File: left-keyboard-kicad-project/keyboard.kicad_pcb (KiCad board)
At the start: 2 copper layers, 180 x 155.4 mm, 78 parts, among them U1 Arduino_Pro_Micro, U2 TRRS

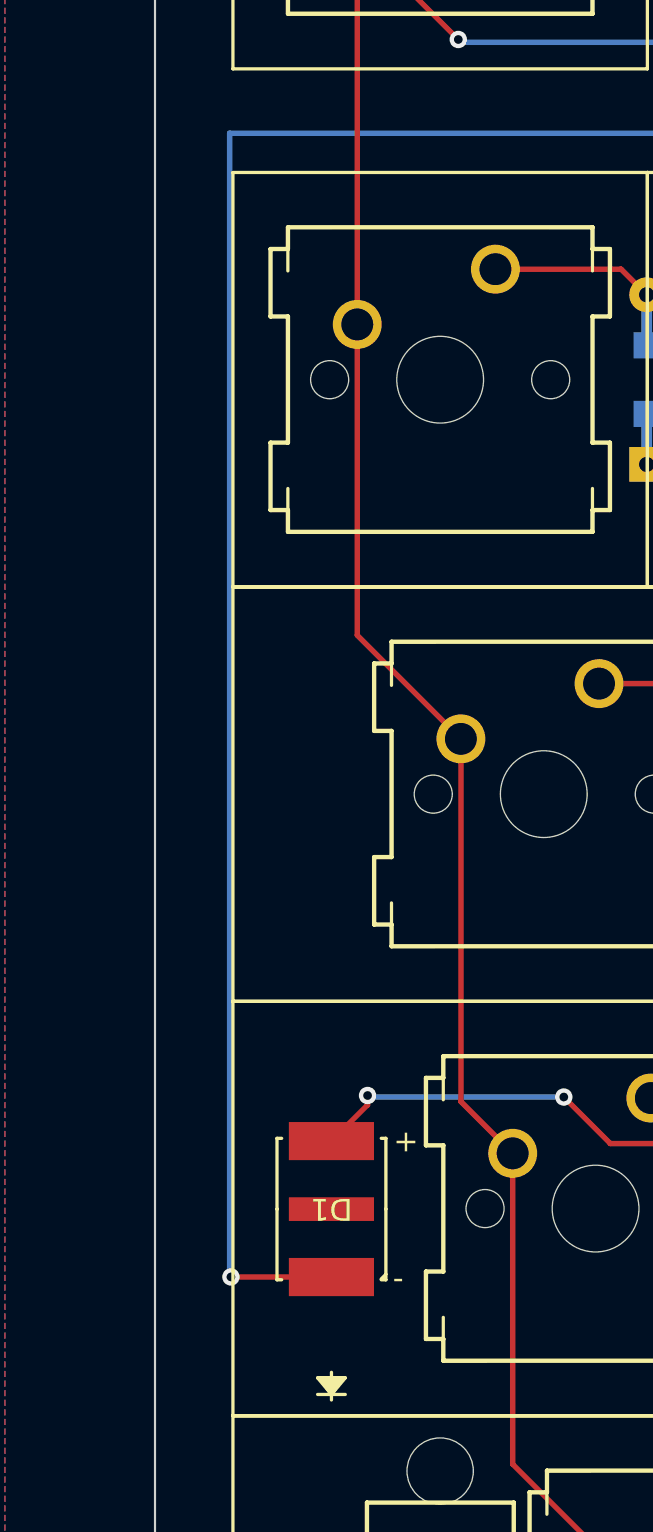
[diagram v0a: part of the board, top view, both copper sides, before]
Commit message: update left keyboard to have slightly shifted LED
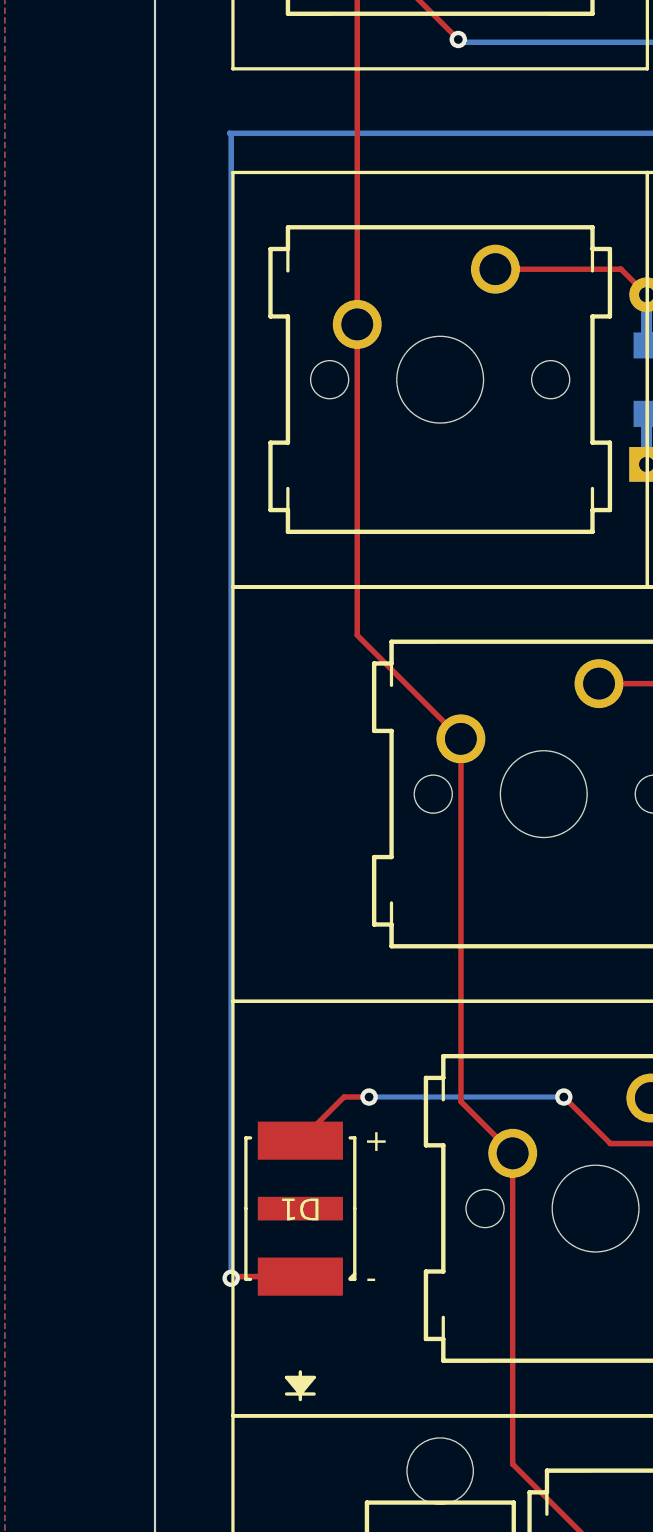
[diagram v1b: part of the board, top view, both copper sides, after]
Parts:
- moved D1 1.43 mm to (51.7, 104.7)
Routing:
- net GND: track 234.0 -> 232.6 mm
- net Net-(D1-A): track 27.8 -> 28.9 mm
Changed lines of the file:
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@@
   )
   (footprint "MX6AWT_A1_0000_000D51 footprint:LED_CREE_MX6" (layer "F.Cu")
-    (at 53.11 104.6794 180)
+    (at 51.68 104.6594 180)
     (tags "MX6AWT-A1-0000-000D51 ")
     (property "Sheetfile" "keyboard.kicad_sch")
@@
   (gr_line (start 212.5 70) (end 197.5 70)
     (stroke (width 0.1) (type default)) (layer "Edge.Cuts"))
-  (gr_text "+" (at 55.96 102.15) (layer "F.SilkS")
+  (gr_text "+" (at 54.6 102.13) (layer "F.SilkS")
     (effects (font (size 1 1) (thickness 0.15)) (justify left bottom))
   )
-  (gr_text "-" (at 55.93 108.44) (layer "F.SilkS")
+  (gr_text "-" (at 54.69 108.43) (layer "F.SilkS")
     (effects (font (size 1 1) (thickness 0.15)) (justify left bottom))
   )
   (segment (start 76.9 101.67) (end 65.93 101.67) (width 0.25) (layer "F.Cu") (net 1))
   (segment (start 65.93 101.67) (end 63.79 99.53) (width 0.25) (layer "F.Cu") (net 1))
-  (segment (start 54.77 99.46) (end 54.77 99.8952) (width 0.25) (layer "F.Cu") (net 1))
-  (segment (start 54.77 99.8952) (end 53.11 101.5552) (width 0.25) (layer "F.Cu") (net 1))
+  (segment (start 51.68 101.5352) (end 53.6852 99.53) (width 0.25) (layer "F.Cu") (net 1))
+  (segment (start 53.6852 99.53) (end 54.84 99.53) (width 0.25) (layer "F.Cu") (net 1))
+  (via (at 54.84 99.53) (size 0.8) (drill 0.4) (layers "F.Cu" "B.Cu") (net 1))
   (via (at 63.79 99.53) (size 0.8) (drill 0.4) (layers "F.Cu" "B.Cu") (net 1))
   (via (at 76.9 101.67) (size 0.8) (drill 0.4) (layers "F.Cu" "B.Cu") (net 1))
-  (via (at 54.77 99.46) (size 0.8) (drill 0.4) (layers "F.Cu" "B.Cu") (net 1))
   (segment (start 76.9 103.68) (end 76.9 101.67) (width 0.25) (layer "B.Cu") (net 1))
   (segment (start 63.79 99.53) (end 54.84 99.53) (width 0.25) (layer "B.Cu") (net 1))
-  (segment (start 54.84 99.53) (end 54.77 99.46) (width 0.25) (layer "B.Cu") (net 1))
   (segment (start 85.527525 61.477525) (end 86.68 62.63) (width 0.25) (layer "F.Cu") (net 2))
   (segment (start 79.697071 61.477525) (end 85.527525 61.477525) (width 0.25) (layer "F.Cu") (net 2))
@@
   (segment (start 208.485 46.025) (end 217.375 46.025) (width 0.25) (layer "F.Cu") (net 57))
   (segment (start 212.24 44.7) (end 207.5 39.96) (width 0.25) (layer "F.Cu") (net 60))
+  (segment (start 48.5764 107.7836) (end 51.68 107.7836) (width 0.25) (layer "F.Cu") (net 60))
   (segment (start 192.26 42.5) (end 192.26 45.04) (width 0.25) (layer "F.Cu") (net 60))
   (segment (start 204.96 42.5) (end 192.26 42.5) (width 0.25) (layer "F.Cu") (net 60))
-  (segment (start 48.49 107.8) (end 48.4936 107.8036) (width 0.25) (layer "F.Cu") (net 60))
   (segment (start 215.2 44.7) (end 212.24 44.7) (width 0.25) (layer "F.Cu") (net 60))
-  (segment (start 48.4936 107.8036) (end 53.11 107.8036) (width 0.25) (layer "F.Cu") (net 60))
   (segment (start 207.5 39.96) (end 204.96 42.5) (width 0.25) (layer "F.Cu") (net 60))
   (segment (start 185.3 45.04) (end 185.27 45.07) (width 0.25) (layer "F.Cu") (net 60))
+  (segment (start 48.5 107.86) (end 48.5764 107.7836) (width 0.25) (layer "F.Cu") (net 60))
   (segment (start 192.26 45.04) (end 185.3 45.04) (width 0.25) (layer "F.Cu") (net 60))
   (via (at 185.27 45.07) (size 0.8) (drill 0.4) (layers "F.Cu" "B.Cu") (net 60))
-  (via (at 48.49 107.8) (size 0.8) (drill 0.4) (layers "F.Cu" "B.Cu") (net 60))
+  (via (at 48.5 107.86) (size 0.8) (drill 0.4) (layers "F.Cu" "B.Cu") (net 60))
   (segment (start 185.27 45.07) (end 185.27 45.43) (width 0.25) (layer "B.Cu") (net 60))
   (segment (start 185.27 45.43) (end 175.47 55.23) (width 0.25) (layer "B.Cu") (net 60))
   (segment (start 175.47 55.23) (end 48.43 55.23) (width 0.25) (layer "B.Cu") (net 60))
-  (segment (start 48.43 55.23) (end 48.43 107.74) (width 0.25) (layer "B.Cu") (net 60))
-  (segment (start 48.43 107.74) (end 48.49 107.8) (width 0.25) (layer "B.Cu") (net 60))
+  (segment (start 48.5 55.3) (end 48.5 107.86) (width 0.25) (layer "B.Cu") (net 60))
+  (segment (start 48.43 55.23) (end 48.5 55.3) (width 0.25) (layer "B.Cu") (net 60))
   (zone (net 0) (net_name "") (layers "F&B.Cu") (hatch edge 0.5)
     (connect_pads (clearance 0.508))

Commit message: update left keyboard
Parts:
- moved U2 1.85 mm to (219.3, 33.4)
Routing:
- net Net-(U1-VCC): track 13.7 -> 15.6 mm
- net Net-(U1-RX1/PD2): track 30.9 -> 32.7 mm
- net Net-(U1-TX0/PD3): track 28.4 -> 30.3 mm
- net GND: track 232.6 -> 231.3 mm
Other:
- board text added: "Designed by Kyle Chiu"
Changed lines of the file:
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@@
   )
   (footprint "ScottoKeebs_Components:TRRS_PJ-320A" (layer "F.Cu")
-    (at 217.5 33.4)
+    (at 219.35 33.3775)
     (property "Sheetfile" "keyboard.kicad_sch")
     (property "Sheetname" "")
@@
   (gr_line (start 212.5 70) (end 197.5 70)
     (stroke (width 0.1) (type default)) (layer "Edge.Cuts"))
+  (gr_text "Designed by Kyle Chiu" (at 45.75 154.2) (layer "F.SilkS")
+    (effects (font (size 1 1) (thickness 0.15)) (justify left bottom))
+  )
   (gr_text "+" (at 54.6 102.13) (layer "F.SilkS")
     (effects (font (size 1 1) (thickness 0.15)) (justify left bottom))
@@
   (segment (start 75.67 81.594009) (end 81.984009 75.28) (width 0.25) (layer "B.Cu") (net 52))
   (segment (start 193.5987 38.7587) (end 192.26 37.42) (width 0.25) (layer "F.Cu") (net 53))
-  (segment (start 219.8 39.6) (end 218.9587 38.7587) (width 0.25) (layer "F.Cu") (net 53))
+  (segment (start 219.7775 39.5775) (end 218.9587 38.7587) (width 0.25) (layer "F.Cu") (net 53))
+  (segment (start 221.65 39.5775) (end 219.7775 39.5775) (width 0.25) (layer "F.Cu") (net 53))
   (segment (start 218.9587 38.7587) (end 193.5987 38.7587) (width 0.25) (layer "F.Cu") (net 53))
+  (segment (start 217.981484 36.5775) (end 217.293984 35.89) (width 0.25) (layer "F.Cu") (net 54))
   (segment (start 197.56 40.14) (end 197.38 39.96) (width 0.25) (layer "F.Cu") (net 54))
+  (segment (start 221.65 36.5775) (end 217.981484 36.5775) (width 0.25) (layer "F.Cu") (net 54))
   (segment (start 197.38 39.96) (end 192.26 39.96) (width 0.25) (layer "F.Cu") (net 54))
   (segment (start 217.293984 35.89) (end 199.76 35.89) (width 0.25) (layer "F.Cu") (net 54))
-  (segment (start 218.003984 36.6) (end 217.293984 35.89) (width 0.25) (layer "F.Cu") (net 54))
-  (segment (start 219.8 36.6) (end 218.003984 36.6) (width 0.25) (layer "F.Cu") (net 54))
   (via (at 199.76 35.89) (size 0.8) (drill 0.4) (layers "F.Cu" "B.Cu") (net 54))
   (via (at 197.56 40.14) (size 0.8) (drill 0.4) (layers "F.Cu" "B.Cu") (net 54))
   (segment (start 197.56 38.09) (end 197.56 40.14) (width 0.25) (layer "B.Cu") (net 54))
   (segment (start 199.76 35.89) (end 197.56 38.09) (width 0.25) (layer "B.Cu") (net 54))
-  (segment (start 217.375 46.025) (end 219.8 43.6) (width 0.25) (layer "F.Cu") (net 57))
-  (segment (start 207.5 45.04) (end 208.485 46.025) (width 0.25) (layer "F.Cu") (net 57))
-  (segment (start 208.485 46.025) (end 217.375 46.025) (width 0.25) (layer "F.Cu") (net 57))
+  (segment (start 219.2025 46.025) (end 208.485 46.025) (width 0.25) (layer "F.Cu") (net 57))
+  (segment (start 221.65 43.5775) (end 219.2025 46.025) (width 0.25) (layer "F.Cu") (net 57))
+  (segment (start 208.485 46.025) (end 207.5 45.04) (width 0.25) (layer "F.Cu") (net 57))
   (segment (start 212.24 44.7) (end 207.5 39.96) (width 0.25) (layer "F.Cu") (net 60))
   (segment (start 48.5764 107.7836) (end 51.68 107.7836) (width 0.25) (layer "F.Cu") (net 60))
@@
   (segment (start 204.96 42.5) (end 192.26 42.5) (width 0.25) (layer "F.Cu") (net 60))
   (segment (start 215.2 44.7) (end 212.24 44.7) (width 0.25) (layer "F.Cu") (net 60))
+  (segment (start 215.2225 44.6775) (end 215.2 44.7) (width 0.25) (layer "F.Cu") (net 60))
   (segment (start 207.5 39.96) (end 204.96 42.5) (width 0.25) (layer "F.Cu") (net 60))
+  (segment (start 217.05 44.6775) (end 215.2225 44.6775) (width 0.25) (layer "F.Cu") (net 60))
   (segment (start 185.3 45.04) (end 185.27 45.07) (width 0.25) (layer "F.Cu") (net 60))
   (segment (start 48.5 107.86) (end 48.5764 107.7836) (width 0.25) (layer "F.Cu") (net 60))
@@
   (via (at 185.27 45.07) (size 0.8) (drill 0.4) (layers "F.Cu" "B.Cu") (net 60))
   (via (at 48.5 107.86) (size 0.8) (drill 0.4) (layers "F.Cu" "B.Cu") (net 60))
-  (segment (start 185.27 45.07) (end 185.27 45.43) (width 0.25) (layer "B.Cu") (net 60))
   (segment (start 185.27 45.43) (end 175.47 55.23) (width 0.25) (layer "B.Cu") (net 60))
-  (segment (start 175.47 55.23) (end 48.43 55.23) (width 0.25) (layer "B.Cu") (net 60))
-  (segment (start 48.5 55.3) (end 48.5 107.86) (width 0.25) (layer "B.Cu") (net 60))
-  (segment (start 48.43 55.23) (end 48.5 55.3) (width 0.25) (layer "B.Cu") (net 60))
+  (segment (start 53.755 55.23) (end 48.52 60.465) (width 0.25) (layer "B.Cu") (net 60))
+  (segment (start 175.47 55.23) (end 53.755 55.23) (width 0.25) (layer "B.Cu") (net 60))
+  (segment (start 48.52 107.84) (end 48.5 107.86) (width 0.25) (layer "B.Cu") (net 60))
+  (segment (start 185.27 45.07) (end 185.27 45.43) (width 0.25) (layer "B.Cu") (net 60))
+  (segment (start 48.52 60.465) (end 48.52 107.84) (width 0.25) (layer "B.Cu") (net 60))
   (zone (net 0) (net_name "") (layers "F&B.Cu") (hatch edge 0.5)
     (connect_pads (clearance 0.508))
